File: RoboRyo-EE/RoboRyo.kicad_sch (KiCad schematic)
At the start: 1 part, among them U1 STM32F446RETx

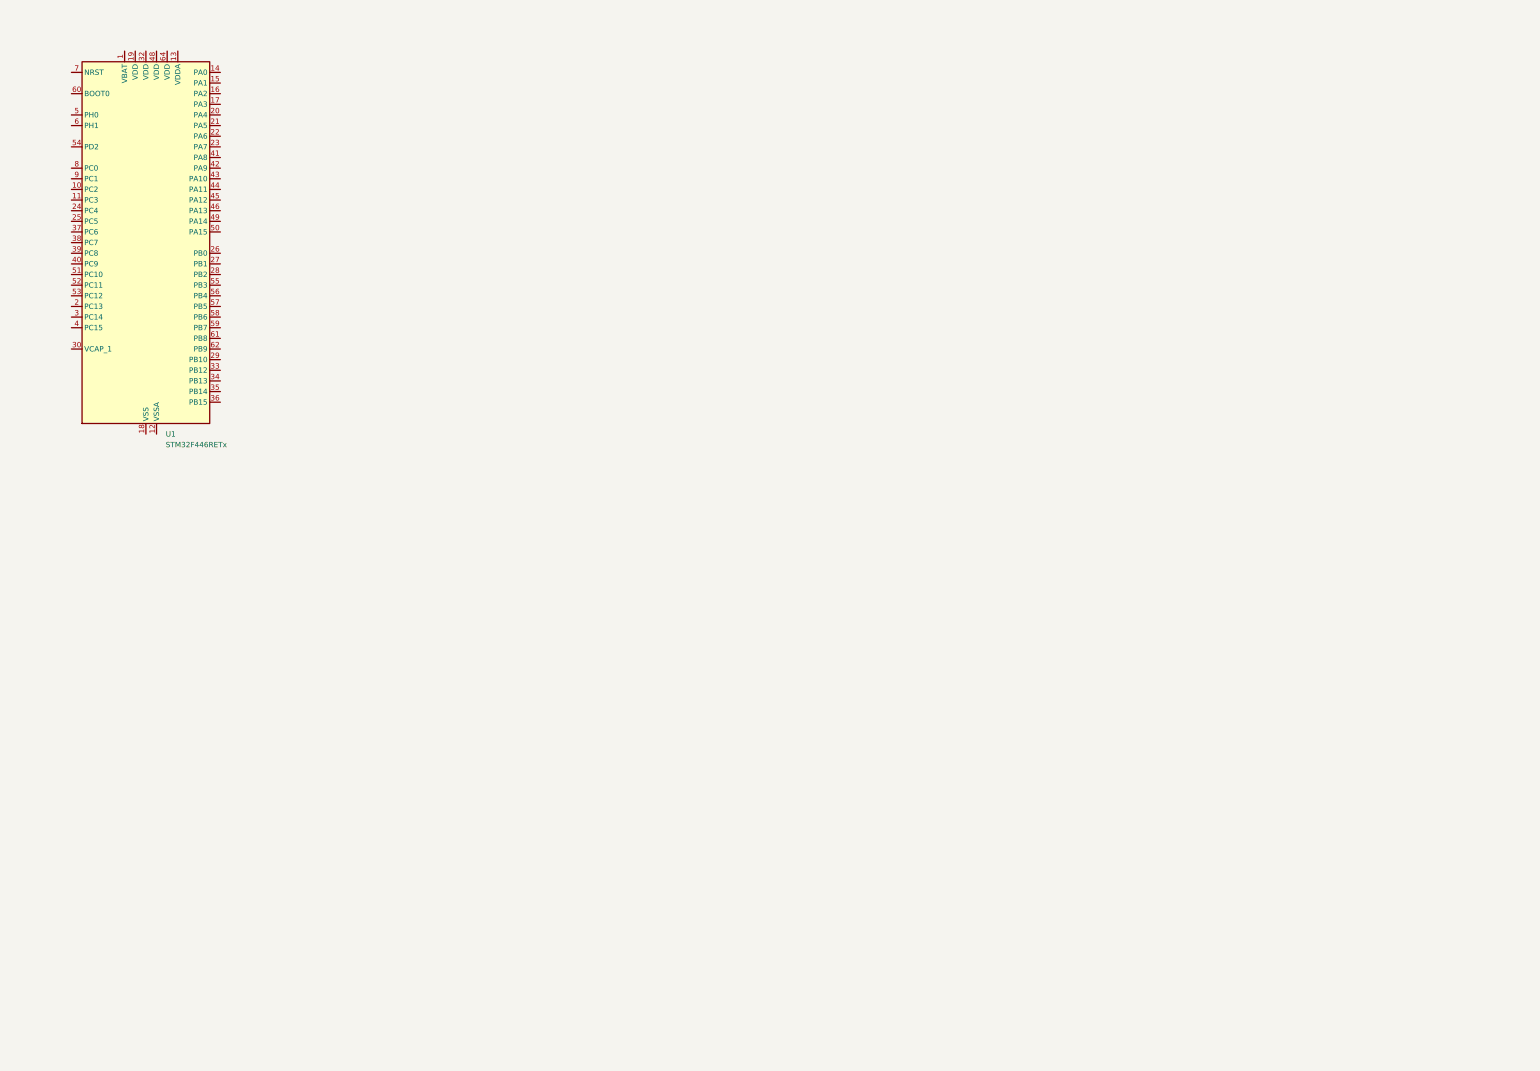
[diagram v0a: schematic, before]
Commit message: Added parts from previous CAD file
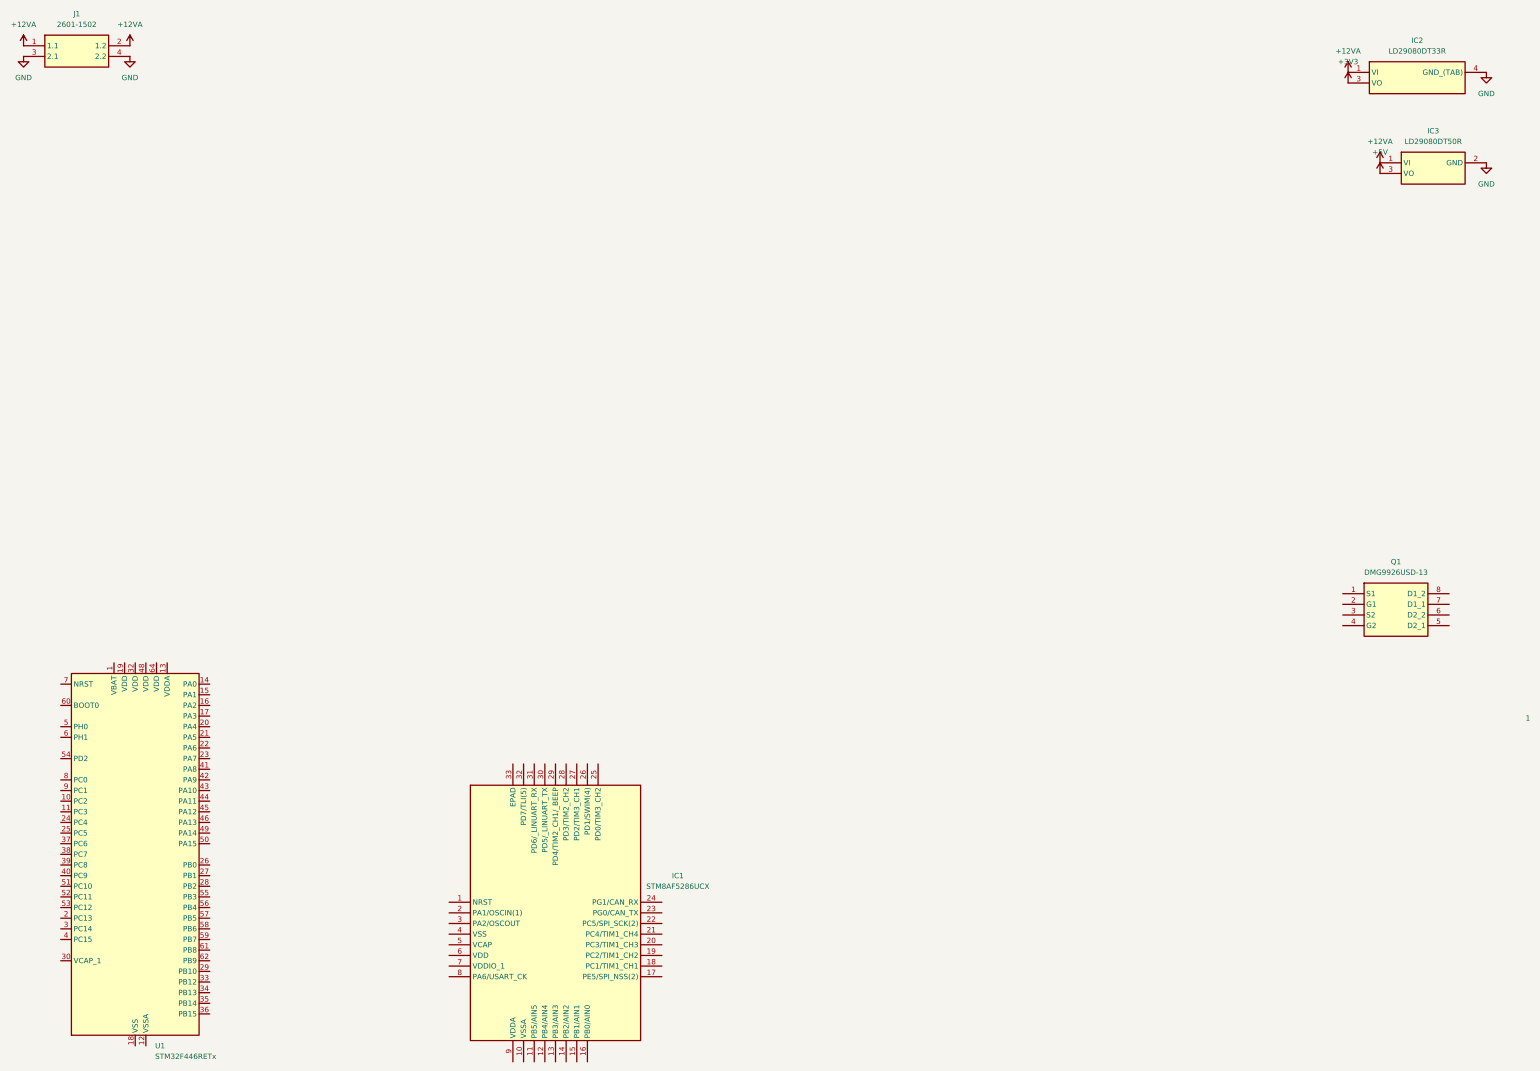
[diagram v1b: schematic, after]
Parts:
- added IC1: STM8AF5286UCX, QFN50P500X500X100-33N-D, symbol SamacSys_Parts:STM8AF5286UCX
- added IC2: LD29080DT33R, TO228P972X240-3N, symbol SamacSys_Parts:LD29080DT33R
- added IC3: LD29080DT50R, LD29080DT50R, symbol SamacSys_Parts:LD29080DT50R
- added J1: 2601-1502, 26011502, symbol SamacSys_Parts:2601-1502
- added Q1: DMG9926USD-13, SOIC127P600X175-8N, symbol SamacSys_Parts:DMG9926USD-13
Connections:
- new net +12VA: IC2.1 (VI), IC3.1 (VI), J1.1 (1.1), J1.2 (1.2)
- new net +3V3: IC2.3 (VO)
- new net +5V: IC3.3 (VO)
- new net GND: IC2.4 (GND_(TAB)), IC3.2 (GND), J1.3 (2.1), J1.4 (2.2)
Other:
- note added: "1"
- company: (none) -> Team 1280 Ragin' C-Biscuit
- title: (none) -> Robo Ryo
- moved on the sheet: U1

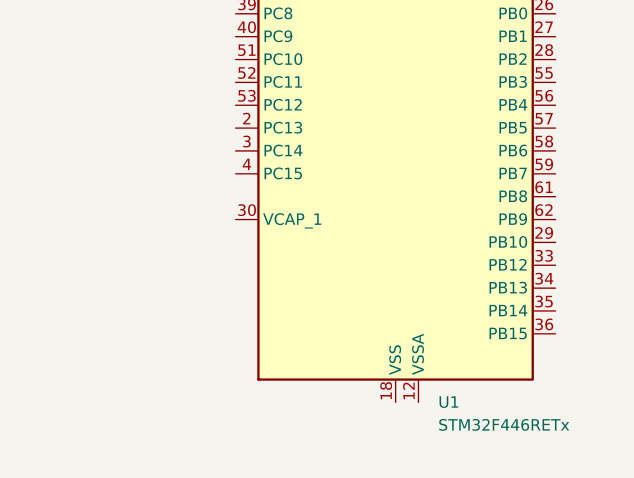
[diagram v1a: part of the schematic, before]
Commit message: Added parts from previous CAD file part 2
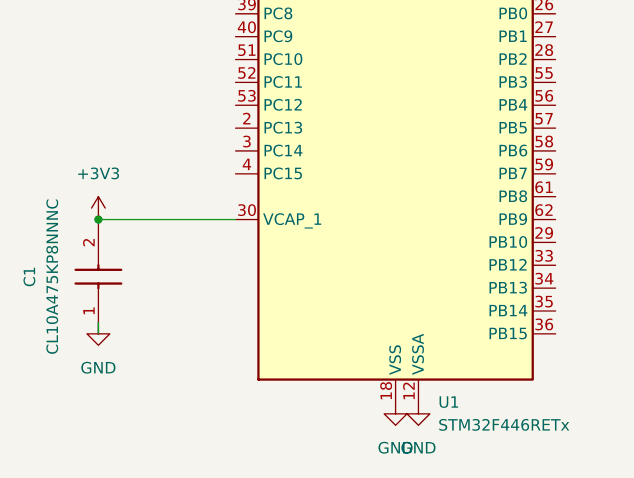
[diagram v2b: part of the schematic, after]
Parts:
- added C1: CL10A475KP8NNNC, CAPC1608X90N, symbol SamacSys_Parts:CL10A475KP8NNNC
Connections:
- net +3V3: now also U1.30 (VCAP_1), C1.2
- net GND: now also U1.12 (VSSA), U1.18 (VSS), U1.31 (VSS), U1.47 (VSS), U1.63 (VSS), C1.1

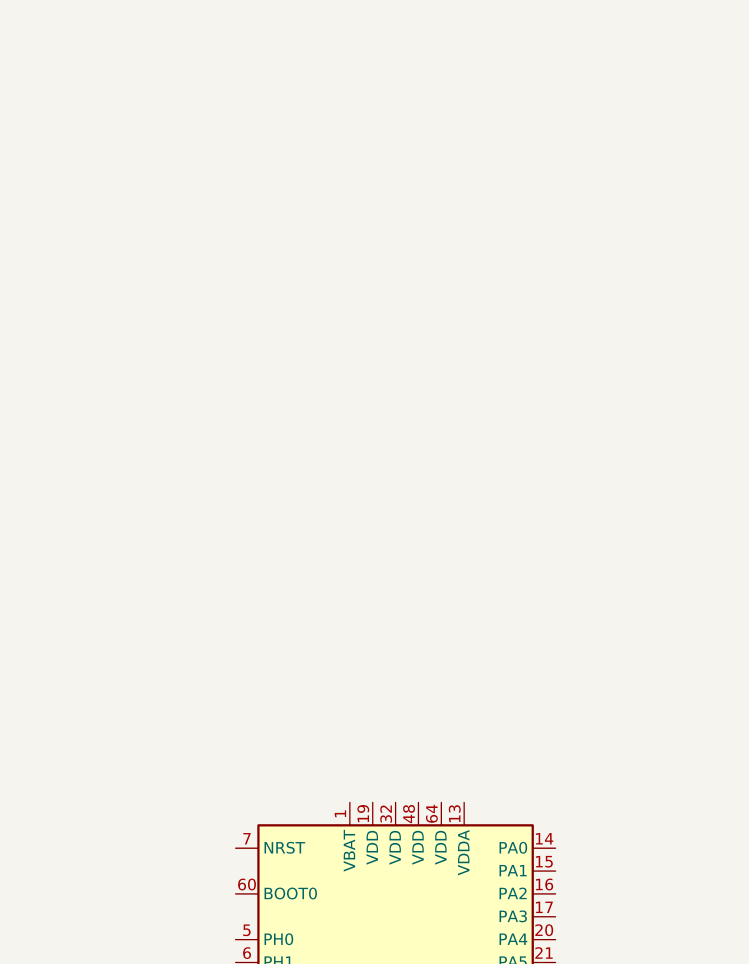
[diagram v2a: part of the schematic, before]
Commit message: added power to STM32F446RETx
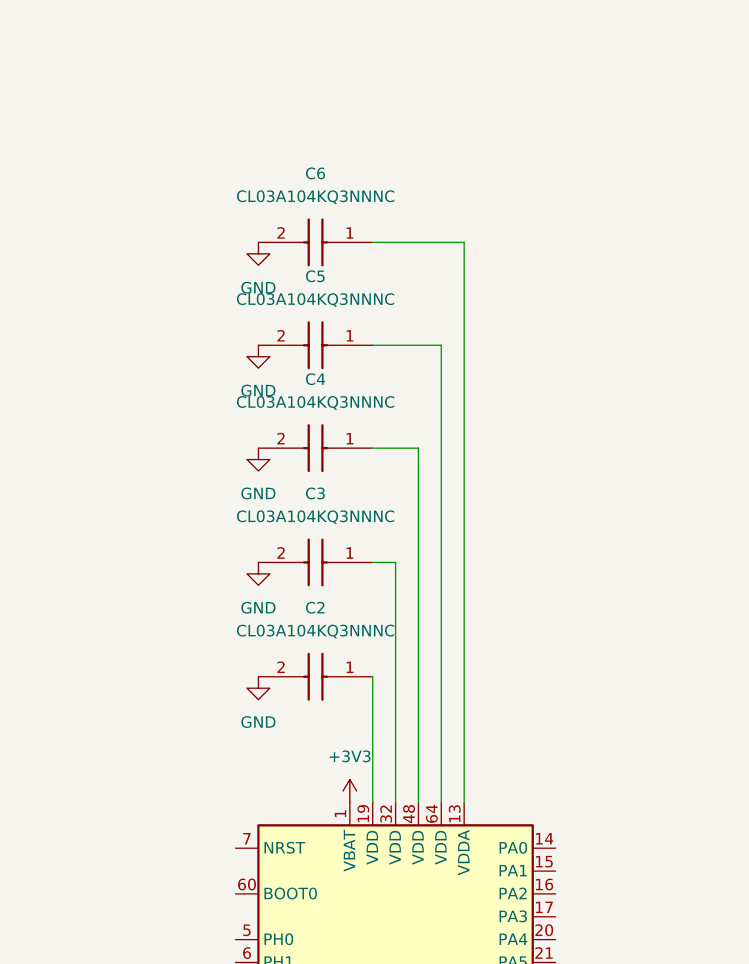
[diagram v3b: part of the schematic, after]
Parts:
- added C2, C3, C4, C5, C6: CL03A104KQ3NNNC, CAPC0603X33N, symbol SamacSys_Parts:CL03A104KQ3NNNC
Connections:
- net +3V3: now also U1.1 (VBAT)
- net GND: now also C2.2, C3.2, C4.2, C5.2, C6.2
- net at U1.13 (VDDA): now also C6.1
- net at U1.19 (VDD): now also C2.1
- net at U1.32 (VDD): now also C3.1
- net at U1.48 (VDD): now also C4.1
- net at U1.64 (VDD): now also C5.1

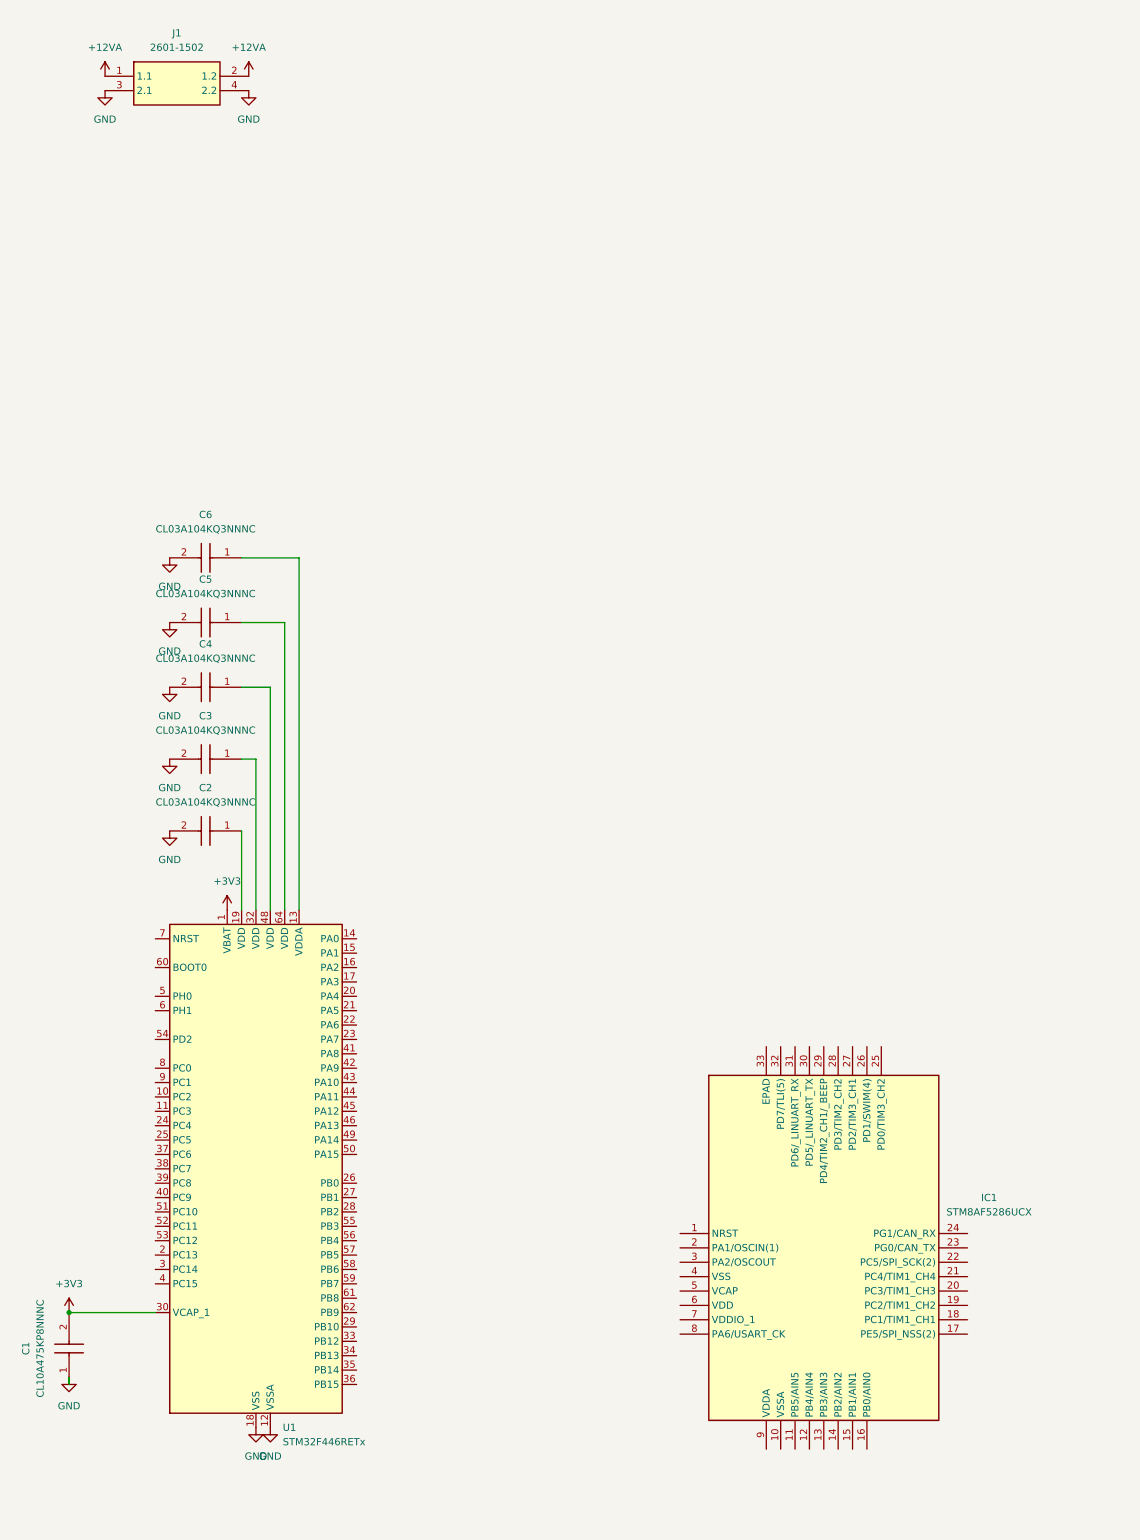
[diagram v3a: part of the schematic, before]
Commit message: added power to STM32F446RETx
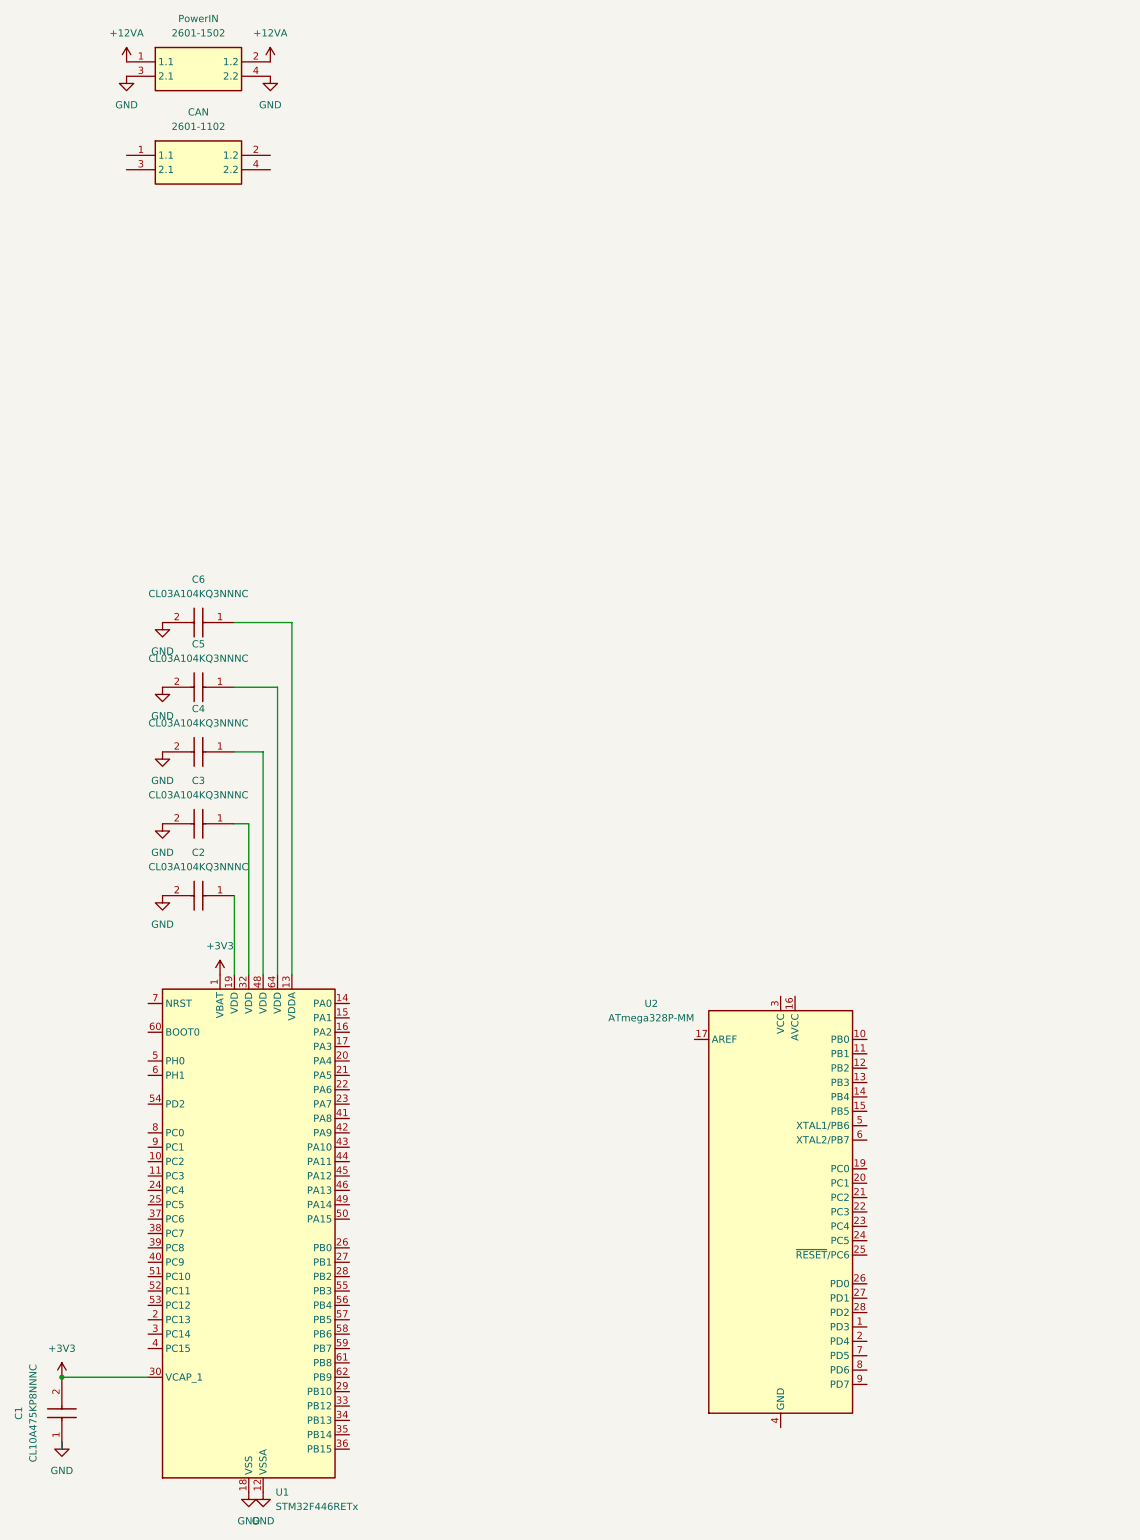
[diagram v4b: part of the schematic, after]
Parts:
- removed IC1: STM8AF5286UCX, QFN50P500X500X100-33N-D, symbol SamacSys_Parts:STM8AF5286UCX
- added CAN: 2601-1102, 26011102, symbol SamacSys_Parts:2601-1102
- added U2: ATmega328P-MM, Package_DFN_QFN:QFN-28-1EP_4x4mm_P0.45mm_EP2.4x2.4mm, symbol MCU_Microchip_ATmega:ATmega328P-MM
- renumbered J1 to PowerIN
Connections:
- new net: U2.18 (GND), U2.29 (GND), U2.4 (GND)
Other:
- moved on the sheet: C1, C2, C3, C4, C5, C6, PowerIN, U1
